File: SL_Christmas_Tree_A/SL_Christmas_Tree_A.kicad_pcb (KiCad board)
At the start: 2 copper layers, 85.7 x 133.1 mm, 60 parts

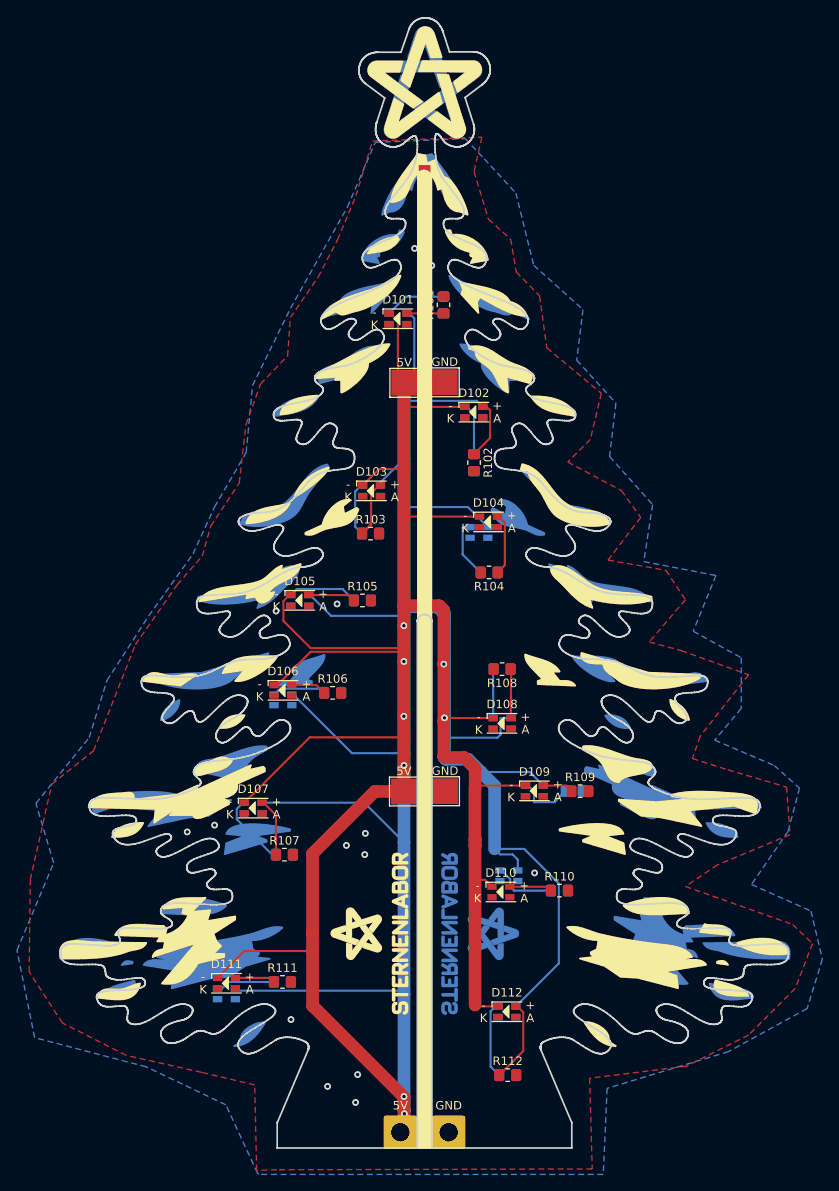
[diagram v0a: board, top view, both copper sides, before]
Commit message: fix swapped 5V / GND
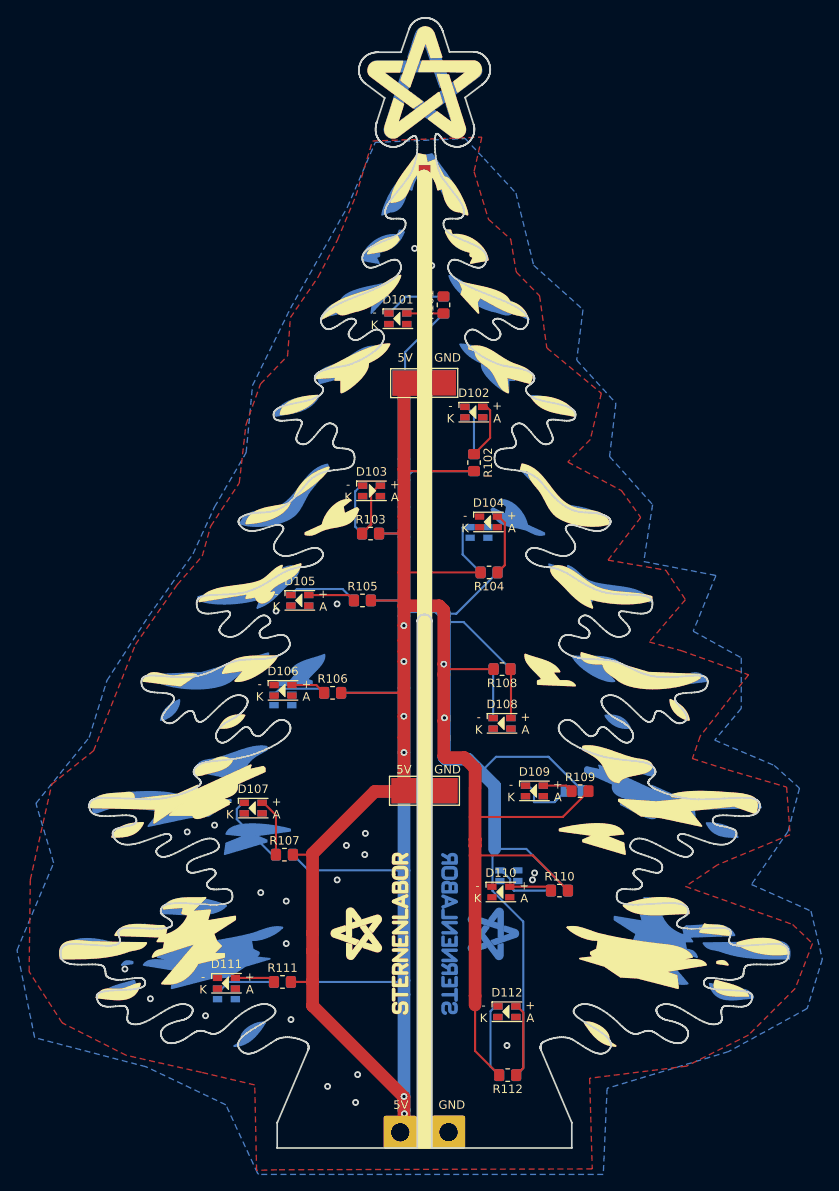
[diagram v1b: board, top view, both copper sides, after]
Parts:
- J101, J201: renamed from 5V; value 5V -> GND
- J102, J202: renamed from GND; value GND -> 5V
- moved J202 5.70 mm to (96.9, 163.7)
- moved J102 5.70 mm to (96.9, 163.7)
- moved J101 5.69 mm to (102.6, 163.7)
- moved J201 5.67 mm to (102.6, 163.7)
- moved GND-101 4.84 mm to (102.2, 123.5)
- moved 5V-101 4.84 mm to (97.4, 123.5)
- moved 5V-202 4.69 mm to (97.5, 123.5)
- moved 5V-201 4.69 mm to (97.5, 75.4)
- moved 5V-102 4.67 mm to (97.5, 75.5)
- moved GND-202 4.63 mm to (102.0, 123.5)
- moved GND-102 4.59 mm to (102.0, 75.5)
- moved GND-201 4.59 mm to (102.0, 75.4)
- turned R112 to 180 degrees
- renumbered GND to 5V-101, GND to 5V-102, GND to 5V-201, GND to 5V-202, 5V to GND-101, 5V to GND-102, 5V to GND-201, 5V to GND-202
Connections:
- 5V-101 pad 1: GND -> +5V
- 5V-102 pad 1: GND -> +5V
- 5V-201 pad 1: GND -> +5V
- 5V-202 pad 1: GND -> +5V
- D101 pad 1: +5V -> GND
- D102 pad 1: +5V -> GND
- D103 pad 1: +5V -> GND
- D104 pad 1: +5V -> GND
- D105 pad 1: +5V -> GND
- D106 pad 1: +5V -> GND
- D107 pad 1: +5V -> GND
- D108 pad 1: +5V -> GND
- D109 pad 1: +5V -> GND
- D110 pad 1: +5V -> GND
- D111 pad 1: +5V -> GND
- D112 pad 1: +5V -> GND
- D201 pad 1: +5V -> GND
- D202 pad 1: +5V -> GND
- D203 pad 1: +5V -> GND
- D204 pad 1: +5V -> GND
- D205 pad 1: +5V -> GND
- D206 pad 1: +5V -> GND
- D207 pad 1: +5V -> GND
- D208 pad 1: +5V -> GND
- D209 pad 1: +5V -> GND
- D210 pad 1: +5V -> GND
- D211 pad 1: +5V -> GND
- D212 pad 1: +5V -> GND
- GND-101 pad 1: +5V -> GND
- GND-102 pad 1: +5V -> GND
- GND-201 pad 1: +5V -> GND
- GND-202 pad 1: +5V -> GND
- J101 pad 1: +5V -> GND
- J102 pad 1: GND -> +5V
- J201 pad 1: +5V -> GND
- J202 pad 1: GND -> +5V
- R101 pad 2: GND -> +5V
- R102 pad 2: GND -> +5V
- R103 pad 2: GND -> +5V
- R104 pad 2: GND -> +5V
- R105 pad 2: GND -> +5V
- R106 pad 2: GND -> +5V
- R107 pad 2: GND -> +5V
- R108 pad 2: GND -> +5V
- R109 pad 2: GND -> +5V
- R110 pad 2: GND -> +5V
- R111 pad 2: GND -> +5V
- R112 pad 2: GND -> +5V
- R201 pad 2: GND -> +5V
- R202 pad 2: GND -> +5V
- R203 pad 2: GND -> +5V
- R204 pad 2: GND -> +5V
- R205 pad 2: GND -> +5V
- R206 pad 2: GND -> +5V
- R207 pad 2: GND -> +5V
- R208 pad 2: GND -> +5V
- R209 pad 2: GND -> +5V
- R210 pad 2: GND -> +5V
- R211 pad 2: GND -> +5V
- R212 pad 2: GND -> +5V
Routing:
- net +5V: track 551.3 -> 503.8 mm
- net GND: track 0.00 -> 2.47 mm, vias 15 -> 24
- net Net-(D112-Pad2): track 9.73 -> 8.90 mm
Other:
- board text added: "5V"
- board text added: "GND"

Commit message: fixes
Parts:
- moved R101 1.96 mm to (102.4, 68.2), turned to -90 degrees
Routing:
- net +5V: track 503.8 -> 513.0 mm
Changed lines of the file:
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@@
   )
   (footprint "Resistor_SMD:R_0805_2012Metric_Pad1.20x1.40mm_HandSolder" (layer "F.Cu")
-    (at 102.02 66.28 90)
+    (at 102.4 68.2 -90)
     (descr "Resistor SMD 0805 (2012 Metric), square (rectangular) end terminal, IPC_7351 nominal with elongated pad for handsoldering. (Body size source: IPC-SM-782 page 72, https://www.pcb-3d.com/wordpress/wp-content/uploads/ipc-sm-782a_amendment_1_and_2.pdf), generated with kicad-footprint-generator")
     (tags "resistor handsolder")
@@
     (fp_line (start 1 -0.625) (end 1 0.625) (layer "F.Fab") (width 0.1))
     (fp_line (start -1 -0.625) (end 1 -0.625) (layer "F.Fab") (width 0.1))
-    (pad "1" smd roundrect (at -1 0 90) (size 1.2 1.4) (layers "F.Cu" "F.Paste" "F.Mask") (roundrect_rratio 0.2083333333)
+    (pad "1" smd roundrect (at -1 0 270) (size 1.2 1.4) (layers "F.Cu" "F.Paste" "F.Mask") (roundrect_rratio 0.2083333333)
       (net 2 "Net-(D101-Pad2)") (pintype "passive"))
-    (pad "2" smd roundrect (at 1 0 90) (size 1.2 1.4) (layers "F.Cu" "F.Paste" "F.Mask") (roundrect_rratio 0.2083333333)
+    (pad "2" smd roundrect (at 1 0 270) (size 1.2 1.4) (layers "F.Cu" "F.Paste" "F.Mask") (roundrect_rratio 0.2083333333)
       (net 1 "+5V") (pintype "passive"))
     (model "${KICAD6_3DMODEL_DIR}/Resistor_SMD.3dshapes/R_0805_2012Metric.wrl"
@@
   (segment (start 97.36 85.61) (end 97.36 76.19) (width 1.5) (layer "F.Cu") (net 1))
   (segment (start 102.06 108.59) (end 102.06 109.81) (width 1.5) (layer "F.Cu") (net 1))
+  (segment (start 102.4 69.2) (end 101 69.2) (width 0.25) (layer "F.Cu") (net 1))
   (segment (start 97.37 163.29) (end 96.94 163.72) (width 1.5) (layer "F.Cu") (net 1))
   (segment (start 89.96 111.97) (end 97.33 111.97) (width 0.25) (layer "F.Cu") (net 1))
@@
   (segment (start 96.6 74.335717) (end 96.64952 74.286197) (width 0.25) (layer "F.Cu") (net 1))
   (segment (start 97.6 85.85) (end 97.36 85.61) (width 0.25) (layer "F.Cu") (net 1))
+  (segment (start 101 69.2) (end 97.5 72.7) (width 0.25) (layer "F.Cu") (net 1))
   (segment (start 107.92 109.18) (end 102.69 109.18) (width 0.25) (layer "F.Cu") (net 1))
   (segment (start 93.92 123.59) (end 86.6 130.91) (width 1.5) (layer "F.Cu") (net 1))
@@
   (segment (start 97.36 123.59) (end 93.92 123.59) (width 1.5) (layer "F.Cu") (net 1))
   (segment (start 116.68 135.26) (end 112.54 131.12) (width 0.25) (layer "F.Cu") (net 1))
+  (segment (start 97.5 72.7) (end 97.5 75.5) (width 0.25) (layer "F.Cu") (net 1))
   (via (at 97.37 119) (size 0.8) (drill 0.4) (layers "F.Cu" "B.Cu") (net 1))
   (via (at 102.06 108.59) (size 0.8) (drill 0.4) (layers "F.Cu" "B.Cu") (net 1))

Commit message: fix Routing
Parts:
- moved D110 8.70 mm to (117.5, 135.0)
- moved R110 5.17 mm to (110.6, 134.5), turned to 180 degrees
- moved R201 1.50 mm to (102.2, 67.8)
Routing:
- net +5V: track 513.0 -> 503.8 mm
- net Net-(D110-Pad2): track 5.04 -> 7.59 mm
- net GND: vias 24 -> 57
